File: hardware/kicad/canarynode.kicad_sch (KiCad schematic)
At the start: 49 parts, among them J1 Conn_01x02, J2 USB_C_Receptacle_USB2.0_16P, J3 Screw_Terminal_01x03, J4 Conn_01x02, SW1 SW_Push, U1 TPS62160DGK, U2 STM32G474RETx, U3 USBLC6-2P6, U4 BMI270, U5 BME280, U6 TCAN334G

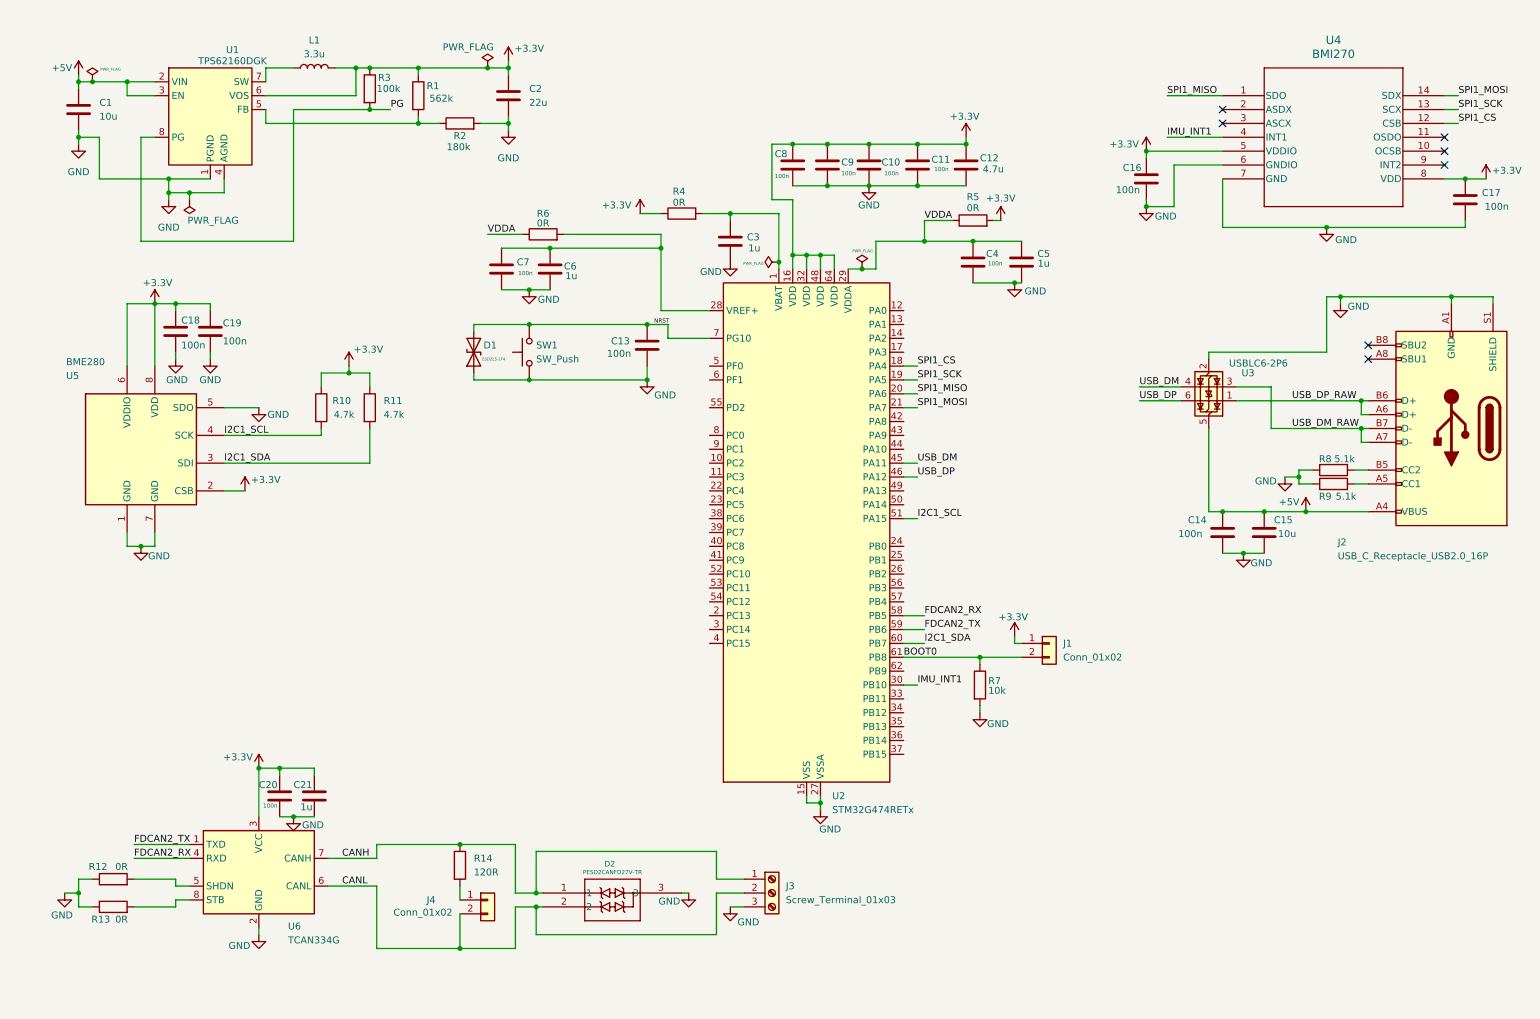
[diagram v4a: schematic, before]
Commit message: v1.0-schematic-complete: pre-layout validation done
- All 9 validation categories cleared
- Footprint fixes: J3 drill 1.4mm, SW1/SW2 swap to C6630024
- I2C1 pin assignment corrected to PA15/PB7
- Board outline 50x60mm, SIG/GND/GND/SIG stackup
- BOM finalized, 61 components
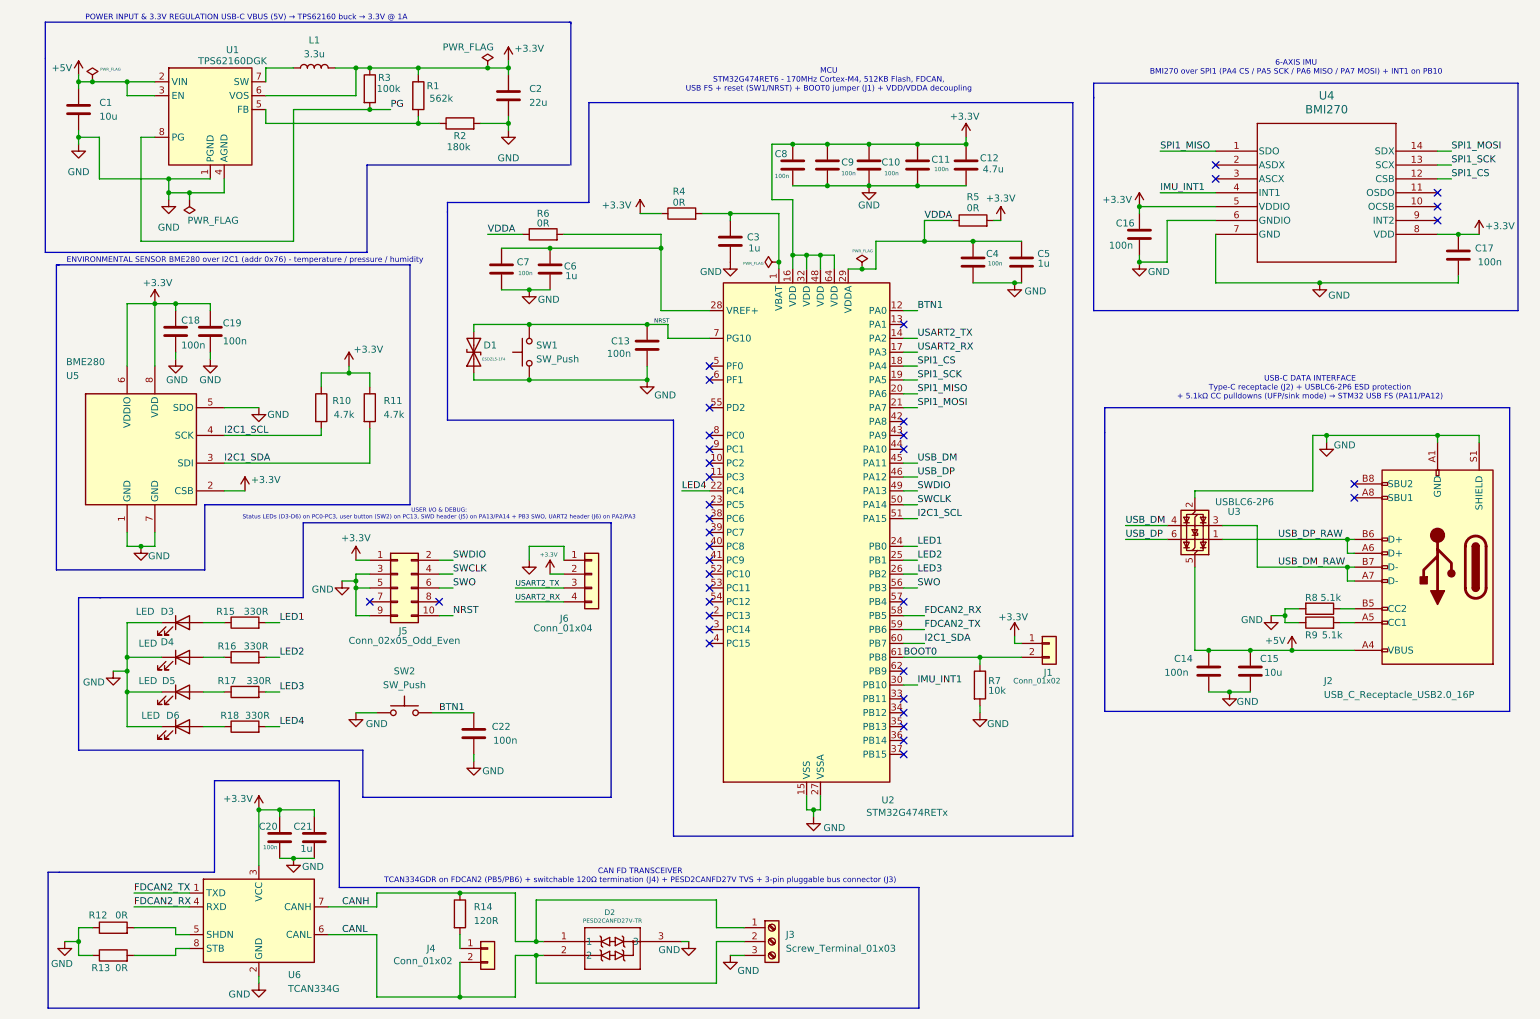
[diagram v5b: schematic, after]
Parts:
- added C22: 100n, Capacitor_SMD:C_0402_1005Metric, symbol Device:C
- added D3, D4, D5, D6: LED, LED_SMD:LED_0603_1608Metric, symbol Device:LED
- added J5: Conn_02x05_Odd_Even, Connector_PinHeader_1.27mm:PinHeader_2x05_P1.27mm_Vertical_SMD, symbol Connector_Generic:Conn_02x05_Odd_Even
- added J6: Conn_01x04, Connector_PinHeader_2.54mm:PinHeader_1x04_P2.54mm_Vertical, symbol Connector_Generic:Conn_01x04
- added R15, R16, R17, R18: 330R, Resistor_SMD:R_0402_1005Metric, symbol Device:R
- added SW2: SW_Push, Button_Switch_SMD:SW_SPST_PTS645Sx43SMTR92, symbol Switch:SW_Push
- C14, C16, C17, C18, C19, C20: footprint (none) -> Capacitor_SMD:C_0402_1005Metric
- C15, C21: footprint (none) -> Capacitor_SMD:C_0603_1608Metric
- D1: footprint (none) -> Diode_SMD:D_0201_0603Metric
- D2: footprint SOT23_PESD2_NEX -> PESD2CANFD27V-TR:SOT23_PESD2_NEX
- J1, J4: footprint (none) -> Connector_PinHeader_2.54mm:PinHeader_1x02_P2.54mm_Vertical
- J2: footprint (none) -> Connector_USB:USB_C_Receptacle_HRO_TYPE-C-31-M-12
- J3: footprint (none) -> BMI270:PhoenixMC_1x03_P3.5_DB2EVC.kicad_mod
- R10, R11, R12, R13, R7, R8, R9: footprint (none) -> Resistor_SMD:R_0402_1005Metric
- R14: footprint (none) -> Resistor_SMD:R_0603_1608Metric
- SW1: footprint (none) -> Button_Switch_SMD:SW_SPST_PTS645Sx43SMTR92
- U4: footprint BMI270_BOS -> BMI270:BMI270_BOS
- U6: footprint (none) -> Package_SO:SOIC-8_3.9x4.9mm_P1.27mm
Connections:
- net +3.3V: now also J5.1 (Pin_1), J6.2 (Pin_2)
- net GND: now also C22.2, D3.1 (K), D4.1 (K), D5.1 (K), D6.1 (K), J5.3 (Pin_3), J5.5 (Pin_5), J5.9 (Pin_9), J6.1 (Pin_1), SW2.1
- net NRST: now also J5.10 (Pin_10)
- net BTN1: now reaches U2.12 (PA0)
- net BTN1: now also C22.1, SW2.2
- net USART2_TX: now reaches U2.14 (PA2)
- net USART2_TX: now also J6.3 (Pin_3)
- net USART2_RX: now reaches U2.17 (PA3)
- net USART2_RX: now also J6.4 (Pin_4)
- net LED4: now reaches U2.22 (PC4)
- net LED4: now also R18.2
- net LED1: now reaches U2.24 (PB0)
- net LED1: now also R15.2
- net LED2: now reaches U2.25 (PB1)
- net LED2: now also R16.2
- net LED3: now reaches U2.26 (PB2)
- net LED3: now also R17.2
- net SWDIO: now reaches U2.49 (PA13)
- net SWDIO: now also J5.2 (Pin_2)
- net SWCLK: now reaches U2.50 (PA14)
- net SWCLK: now also J5.4 (Pin_4)
- net SWO: now reaches U2.56 (PB3)
- net SWO: now also J5.6 (Pin_6)
- new net: D5.2 (A), R17.1
- new net: D6.2 (A), R18.1
- new net: D4.2 (A), R16.1
- new net: D3.2 (A), R15.1
- no-connect marks 7 -> 38
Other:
- note added: "6-AXIS IMU BMI270 over SPI1 (PA4 CS / PA5 SCK / PA6 MISO / PA7 MOSI) + INT1 on PB10"
- note added: "CAN FD TRANSCEIVER TCAN334GDR on FDCAN2 (PB5/PB6) + switchable 120Ω termination (J4) + PESD2CANFD27V TVS + 3-pin pluggable bus connector (J3)"
- note added: "ENVIRONMENTAL SENSOR BME280 over I2C1 (addr 0x76) - temperature / pressure / humidity"
- note added: "MCU STM32G474RET6 - 170MHz Cortex-M4, 512KB Flash, FDCAN, USB FS + reset (SW1/NRST) + BOOT0 jumper (J1) + VDD/VDDA decoupling"
- note added: "POWER INPUT & 3.3V REGULATION USB-C VBUS (5V) → TPS62160 buck → 3.3V @ 1A"
- note added: "USB-C DATA INTERFACE Type-C receptacle (J2) + USBLC6-2P6 ESD protection + 5.1kΩ CC pulldowns (UFP/sink mode) → STM32 USB FS (PA11/PA12)"
- note added: "USER I/O & DEBUG: Status LEDs (D3-D6) on PC0-PC3, user button (SW2) on PC13, SWD header (J5) on PA13/PA14 + PB3 SWO, UART2 header (J6) on PA2/PA3"
- moved on the sheet: C14, C15, C16, C17, C20, C21, D2, J2, J3, J4, R12, R13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

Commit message: docs(sch): add annotation labels for J1 BOOT0, J4 CAN term, BME280 addr strap
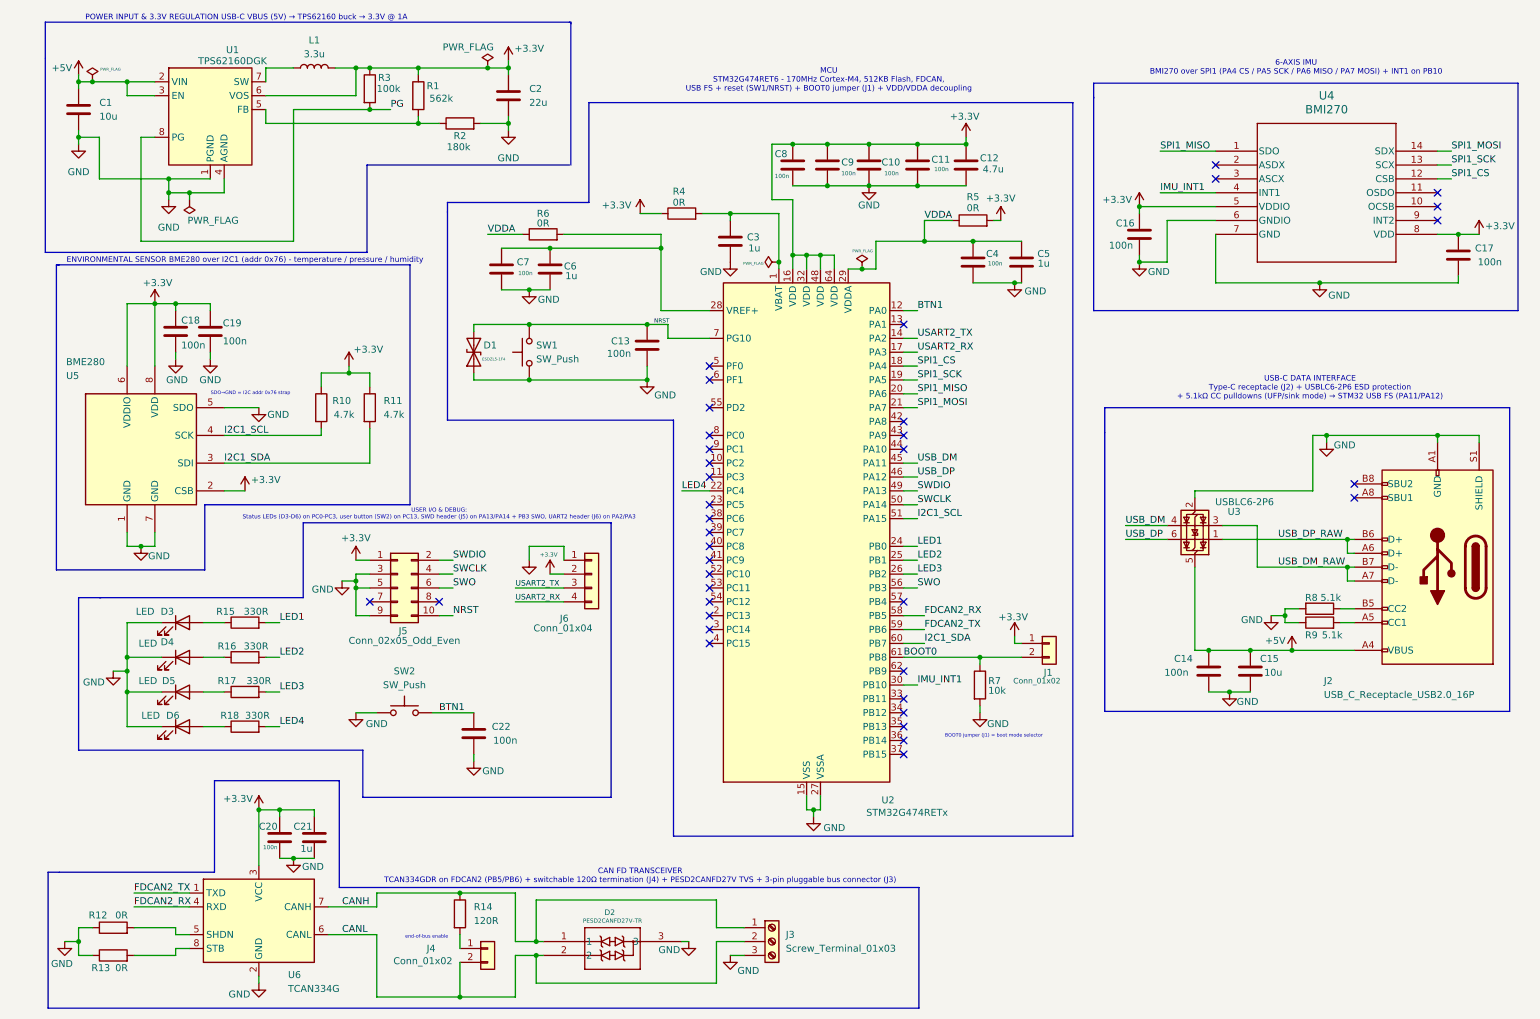
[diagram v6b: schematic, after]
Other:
- note added: "BOOT0 jumper (J1) = boot mode selector"
- note added: "SDO→GND = I2C addr 0x76 strap"
- note added: "end-of-bus enable"
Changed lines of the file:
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@@
 		(comment 1 "Custom CAN sensor node: STM32G474 + IMU + environmental + USB")
+	)
+	(text "BOOT0 jumper (J1) = boot mode selector"
+		(exclude_from_sim no)
+		(at 186.69 145.288 0)
+		(effects
+			(font
+				(size 0.635 0.635)
+			)
+		)
 	)
 	(text "POWER INPUT & 3.3V REGULATION USB-C VBUS (5V) → TPS62160 buck → 3.3V @ 1A"
@@
 		)
 	)
+	(text "end-of-bus enable"
+		(exclude_from_sim no)
+		(at 82.804 182.118 0)
+		(effects
+			(font
+				(size 0.635 0.635)
+			)
+		)
+	)
 	(text "CAN FD TRANSCEIVER\nTCAN334GDR on FDCAN2 (PB5/PB6) + switchable 120Ω termination (J4) + PESD2CANFD27V TVS + 3-pin pluggable bus connector (J3)"
 		(exclude_from_sim no)
@@
 			)
 		)
+	)
+	(text "SDO→GND = I2C addr 0x76 strap"
+		(exclude_from_sim no)
+		(at 50.546 82.55 0)
+		(effects
+			(font
+				(size 0.635 0.635)
+			)
+		)

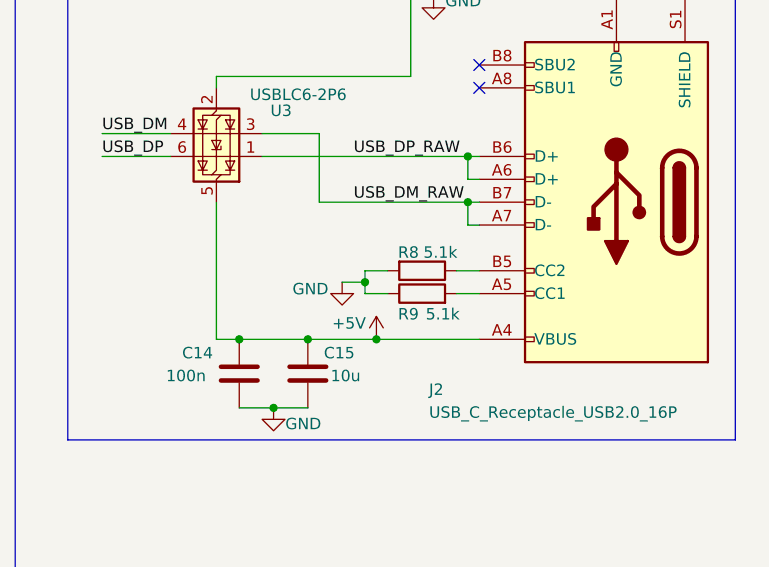
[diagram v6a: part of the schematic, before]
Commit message: fab: add LCSC to BOM, generate CPL, exclude mounting holes from placement, remove stale datasheet
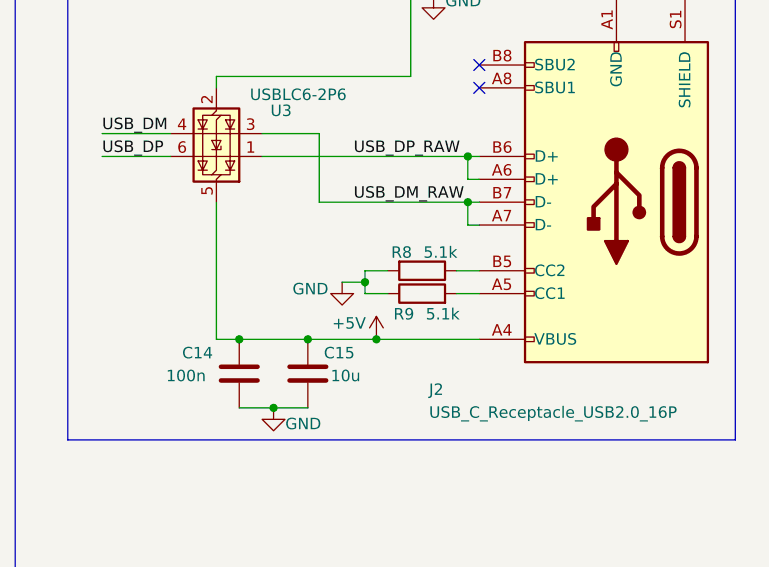
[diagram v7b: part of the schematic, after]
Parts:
- C1, C15: LCSC (none) -> C19702
- C10, C11, C13, C14, C16, C17, C18, C19, C20, C22, C4, C7, C8, C9: LCSC (none) -> C1525
- C12: LCSC (none) -> C19666
- C2: LCSC (none) -> C59461
- C21, C3, C5, C6: LCSC (none) -> C15849
- D1: LCSC (none) -> C2970171
- D2: LCSC (none) -> C552488
- D3: LCSC (none) -> C2286
- D4, D6: LCSC (none) -> C2287
- D5: LCSC (none) -> C2289
- J1, J4: LCSC (none) -> C41417359
- J2: LCSC (none) -> C165948
- J3: LCSC (none) -> C430550
- J5: LCSC (none) -> C4943297
- J6: LCSC (none) -> C41417361
- L1: LCSC (none) -> C3911580
- R1: LCSC (none) -> C48838
- R10, R11: LCSC (none) -> C25900
- R12, R13, R4, R5, R6: LCSC (none) -> C17168
- R14: LCSC (none) -> C22787
- R15, R16, R17, R18: LCSC (none) -> C25104
- R2: LCSC (none) -> C25760
- R3: LCSC (none) -> C25741
- R7: LCSC (none) -> C25744
- R8, R9: LCSC (none) -> C25905
- SW1, SW2: LCSC (none) -> C6630024
- U1: LCSC (none) -> C60726
- U2: LCSC (none) -> C521608
- U3: LCSC (none) -> C15999
- U4: LCSC (none) -> C2836813
- U5: LCSC (none) -> C92489
- U6: LCSC (none) -> C189939
